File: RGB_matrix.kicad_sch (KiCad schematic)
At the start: 117 parts

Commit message: some layouts done
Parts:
- removed D100, D101, D102, D103, D104, D105, D106, D107, D108, D109, D110, D111, D112, D113, D114, D115, D116, D117, D118, D119, D120, D121, D122, D123, D124, D125, D126, D127, D128, D129, D130, D131, D132, D133, D134, D135, D136, D137, D138, D139, D140, D141, D142, D143, D144, D145, D146, D147, D148, D149, D150, D151, D152, D153, D154, D155, D156, D157, D158, D159, D160, D161, D162, D163, D164, D165, D166, D167, D168, D169, D170, D171, D172, D173, D174, D175, D176, D177, D178, D179, D180, D181, D182, D183, D184, D185, D186, D187, D188, D189, D190, D191, D192, D193, D194, D195, D196, D197, D198, D199, D200, D201, D202, D203, D204, D205, D98, D99: LED_ABGR, symbol Device:LED_ABGR
- added RGB10, RGB11, RGB12, RGB13, RGB14, RGB15, RGB16, RGB17, RGB18, RGB19, RGB20, RGB21, RGB22, RGB23, RGB24, RGB25, RGB26, RGB27, RGB28, RGB29, RGB30, RGB31, RGB32, RGB33, RGB34, RGB35, RGB36, RGB37, RGB38, RGB39, RGB40, RGB41, RGB42, RGB43, RGB44, RGB45, RGB46, RGB47, RGB48, RGB49, RGB50, RGB51, RGB52, RGB53, RGB54, RGB55, RGB56, RGB57, RGB58, RGB59, RGB60, RGB61, RGB62, RGB63, RGB64, RGB65, RGB66, RGB67, RGB68, RGB69, RGB70, RGB71, RGB72, RGB73, RGB74, RGB75, RGB76, RGB77, RGB78, RGB79, RGB80, RGB82, RGB83, RGB84, RGB85, RGB86, RGB87, RGB88: LED_ABGR, marbastlib-various:MHT151RGBCT-RGB-Reverse-Mount-1206, symbol Device:LED_ABGR
- RGB1: renamed from D89; footprint (none) -> marbastlib-various:MHT151RGBCT-RGB-Reverse-Mount-1206
- RGB2: renamed from D90; footprint (none) -> marbastlib-various:MHT151RGBCT-RGB-Reverse-Mount-1206
- RGB3: renamed from D91; footprint (none) -> marbastlib-various:MHT151RGBCT-RGB-Reverse-Mount-1206
- RGB4: renamed from D92; footprint (none) -> marbastlib-various:MHT151RGBCT-RGB-Reverse-Mount-1206
- RGB5: renamed from D93; footprint (none) -> marbastlib-various:MHT151RGBCT-RGB-Reverse-Mount-1206
- RGB6: renamed from D94; footprint (none) -> marbastlib-various:MHT151RGBCT-RGB-Reverse-Mount-1206
- RGB7: renamed from D95; footprint (none) -> marbastlib-various:MHT151RGBCT-RGB-Reverse-Mount-1206
- RGB8: renamed from D96; footprint (none) -> marbastlib-various:MHT151RGBCT-RGB-Reverse-Mount-1206
- RGB9: renamed from D97; footprint (none) -> marbastlib-various:MHT151RGBCT-RGB-Reverse-Mount-1206
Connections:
- net CS4: now also RGB10.4 (RK), RGB11.4 (RK), RGB12.4 (RK), RGB13.4 (RK), RGB14.4 (RK), RGB15.4 (RK), RGB16.4 (RK), RGB17.4 (RK), RGB18.4 (RK)
- net CS5: now also RGB10.3 (GK), RGB11.3 (GK), RGB12.3 (GK), RGB13.3 (GK), RGB14.3 (GK), RGB15.3 (GK), RGB16.3 (GK), RGB17.3 (GK), RGB18.3 (GK)
- net CS6: now also RGB10.2 (BK), RGB11.2 (BK), RGB12.2 (BK), RGB13.2 (BK), RGB14.2 (BK), RGB15.2 (BK), RGB16.2 (BK), RGB17.2 (BK), RGB18.2 (BK)
- net SW1: now also RGB10.1 (A), RGB19.1 (A), RGB28.1 (A), RGB37.1 (A), RGB46.1 (A), RGB55.1 (A), RGB64.1 (A), RGB73.1 (A), RGB83.1 (A)
- net SW2: now also RGB11.1 (A), RGB20.1 (A), RGB29.1 (A), RGB38.1 (A), RGB47.1 (A), RGB56.1 (A), RGB65.1 (A), RGB74.1 (A), RGB84.1 (A)
- net SW3: now also RGB12.1 (A), RGB21.1 (A), RGB30.1 (A), RGB39.1 (A), RGB48.1 (A), RGB57.1 (A), RGB66.1 (A), RGB75.1 (A), RGB85.1 (A)
- net SW4: now also RGB13.1 (A), RGB22.1 (A), RGB31.1 (A), RGB40.1 (A), RGB49.1 (A), RGB58.1 (A), RGB67.1 (A), RGB76.1 (A), RGB86.1 (A)
- net SW5: now also RGB14.1 (A), RGB23.1 (A), RGB32.1 (A), RGB41.1 (A), RGB50.1 (A), RGB59.1 (A), RGB68.1 (A), RGB77.1 (A), RGB87.1 (A)
- net SW6: now also RGB15.1 (A), RGB24.1 (A), RGB33.1 (A), RGB42.1 (A), RGB51.1 (A), RGB60.1 (A), RGB69.1 (A), RGB78.1 (A), RGB88.1 (A)
- net SW7: now also RGB16.1 (A), RGB25.1 (A), RGB34.1 (A), RGB43.1 (A), RGB52.1 (A), RGB61.1 (A), RGB70.1 (A), RGB79.1 (A)
- net SW8: now also RGB17.1 (A), RGB26.1 (A), RGB35.1 (A), RGB44.1 (A), RGB53.1 (A), RGB62.1 (A), RGB71.1 (A), RGB80.1 (A)
- net SW9: now also RGB18.1 (A), RGB27.1 (A), RGB36.1 (A), RGB45.1 (A), RGB54.1 (A), RGB63.1 (A), RGB72.1 (A), RGB82.1 (A)
- new net CS10: RGB28.4 (RK), RGB29.4 (RK), RGB30.4 (RK), RGB31.4 (RK), RGB32.4 (RK), RGB33.4 (RK), RGB34.4 (RK), RGB35.4 (RK), RGB36.4 (RK)
- new net CS11: RGB28.3 (GK), RGB29.3 (GK), RGB30.3 (GK), RGB31.3 (GK), RGB32.3 (GK), RGB33.3 (GK), RGB34.3 (GK), RGB35.3 (GK), RGB36.3 (GK)
- new net CS12: RGB28.2 (BK), RGB29.2 (BK), RGB30.2 (BK), RGB31.2 (BK), RGB32.2 (BK), RGB33.2 (BK), RGB34.2 (BK), RGB35.2 (BK), RGB36.2 (BK)
- new net CS13: RGB37.4 (RK), RGB38.4 (RK), RGB39.4 (RK), RGB40.4 (RK), RGB41.4 (RK), RGB42.4 (RK), RGB43.4 (RK), RGB44.4 (RK), RGB45.4 (RK)
- new net CS14: RGB37.3 (GK), RGB38.3 (GK), RGB39.3 (GK), RGB40.3 (GK), RGB41.3 (GK), RGB42.3 (GK), RGB43.3 (GK), RGB44.3 (GK), RGB45.3 (GK)
- new net CS15: RGB37.2 (BK), RGB38.2 (BK), RGB39.2 (BK), RGB40.2 (BK), RGB41.2 (BK), RGB42.2 (BK), RGB43.2 (BK), RGB44.2 (BK), RGB45.2 (BK)
- new net CS16: RGB46.4 (RK), RGB47.4 (RK), RGB48.4 (RK), RGB49.4 (RK), RGB50.4 (RK), RGB51.4 (RK), RGB52.4 (RK), RGB53.4 (RK), RGB54.4 (RK)
- new net CS17: RGB46.3 (GK), RGB47.3 (GK), RGB48.3 (GK), RGB49.3 (GK), RGB50.3 (GK), RGB51.3 (GK), RGB52.3 (GK), RGB53.3 (GK), RGB54.3 (GK)
- new net CS18: RGB46.2 (BK), RGB47.2 (BK), RGB48.2 (BK), RGB49.2 (BK), RGB50.2 (BK), RGB51.2 (BK), RGB52.2 (BK), RGB53.2 (BK), RGB54.2 (BK)
- new net CS19: RGB55.4 (RK), RGB56.4 (RK), RGB57.4 (RK), RGB58.4 (RK), RGB59.4 (RK), RGB60.4 (RK), RGB61.4 (RK), RGB62.4 (RK), RGB63.4 (RK)
- new net CS20: RGB55.3 (GK), RGB56.3 (GK), RGB57.3 (GK), RGB58.3 (GK), RGB59.3 (GK), RGB60.3 (GK), RGB61.3 (GK), RGB62.3 (GK), RGB63.3 (GK)
- new net CS21: RGB55.2 (BK), RGB56.2 (BK), RGB57.2 (BK), RGB58.2 (BK), RGB59.2 (BK), RGB60.2 (BK), RGB61.2 (BK), RGB62.2 (BK), RGB63.2 (BK)
- new net CS22: RGB64.4 (RK), RGB65.4 (RK), RGB66.4 (RK), RGB67.4 (RK), RGB68.4 (RK), RGB69.4 (RK), RGB70.4 (RK), RGB71.4 (RK), RGB72.4 (RK)
- new net CS23: RGB64.3 (GK), RGB65.3 (GK), RGB66.3 (GK), RGB67.3 (GK), RGB68.3 (GK), RGB69.3 (GK), RGB70.3 (GK), RGB71.3 (GK), RGB72.3 (GK)
- new net CS24: RGB64.2 (BK), RGB65.2 (BK), RGB66.2 (BK), RGB67.2 (BK), RGB68.2 (BK), RGB69.2 (BK), RGB70.2 (BK), RGB71.2 (BK), RGB72.2 (BK)
- new net CS25: RGB73.4 (RK), RGB74.4 (RK), RGB75.4 (RK), RGB76.4 (RK), RGB77.4 (RK), RGB78.4 (RK), RGB79.4 (RK), RGB80.4 (RK), RGB82.4 (RK)
- new net CS26: RGB73.3 (GK), RGB74.3 (GK), RGB75.3 (GK), RGB76.3 (GK), RGB77.3 (GK), RGB78.3 (GK), RGB79.3 (GK), RGB80.3 (GK), RGB82.3 (GK)
- new net CS27: RGB73.2 (BK), RGB74.2 (BK), RGB75.2 (BK), RGB76.2 (BK), RGB77.2 (BK), RGB78.2 (BK), RGB79.2 (BK), RGB80.2 (BK), RGB82.2 (BK)
- new net CS28: RGB83.4 (RK), RGB84.4 (RK), RGB85.4 (RK), RGB86.4 (RK), RGB87.4 (RK), RGB88.4 (RK)
- new net CS29: RGB83.3 (GK), RGB84.3 (GK), RGB85.3 (GK), RGB86.3 (GK), RGB87.3 (GK), RGB88.3 (GK)
- new net CS30: RGB83.2 (BK), RGB84.2 (BK), RGB85.2 (BK), RGB86.2 (BK), RGB87.2 (BK), RGB88.2 (BK)
- new net CS7: RGB19.4 (RK), RGB20.4 (RK), RGB21.4 (RK), RGB22.4 (RK), RGB23.4 (RK), RGB24.4 (RK), RGB25.4 (RK), RGB26.4 (RK), RGB27.4 (RK)
- new net CS8: RGB19.3 (GK), RGB20.3 (GK), RGB21.3 (GK), RGB22.3 (GK), RGB23.3 (GK), RGB24.3 (GK), RGB25.3 (GK), RGB26.3 (GK), RGB27.3 (GK)
- new net CS9: RGB19.2 (BK), RGB20.2 (BK), RGB21.2 (BK), RGB22.2 (BK), RGB23.2 (BK), RGB24.2 (BK), RGB25.2 (BK), RGB26.2 (BK), RGB27.2 (BK)

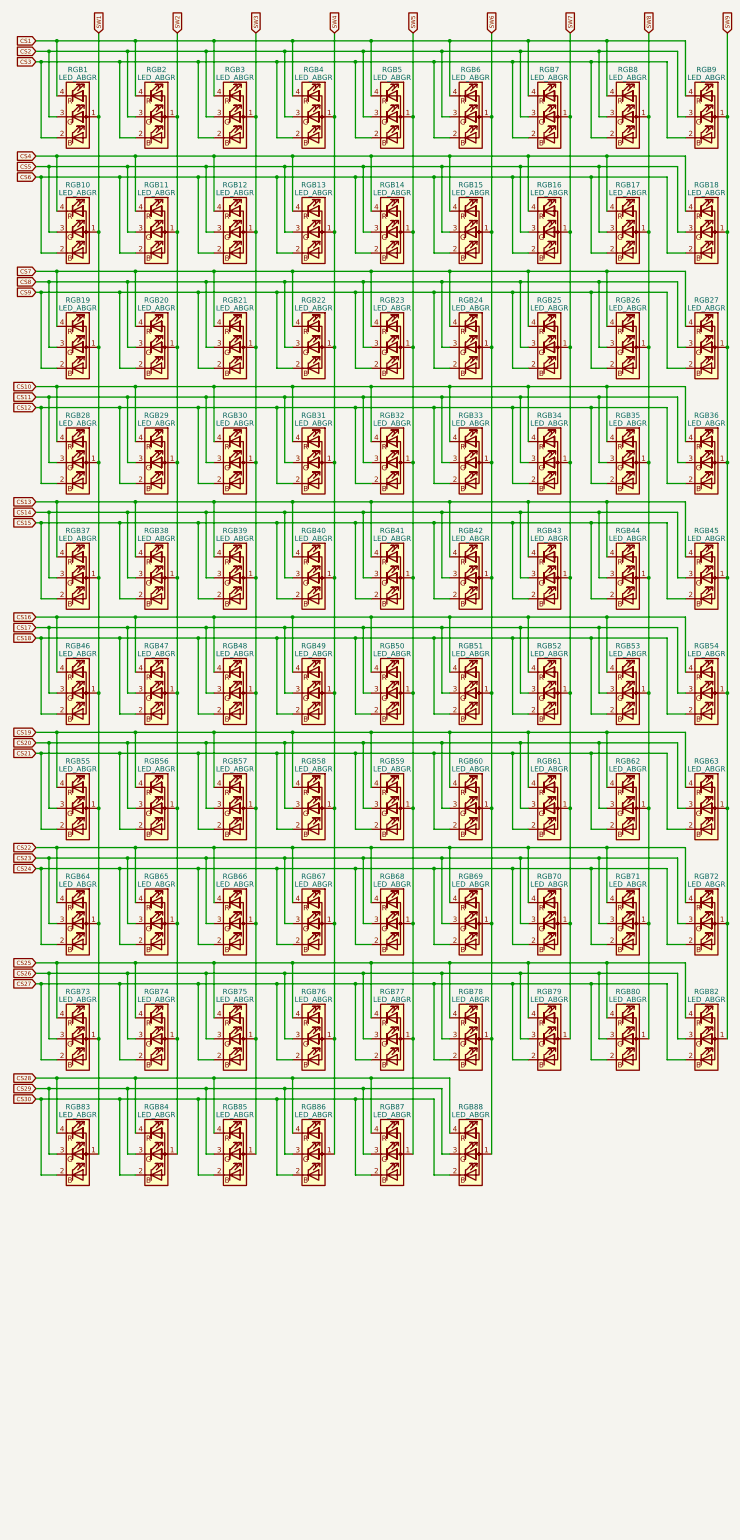
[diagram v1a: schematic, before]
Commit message: improved rgb schematic
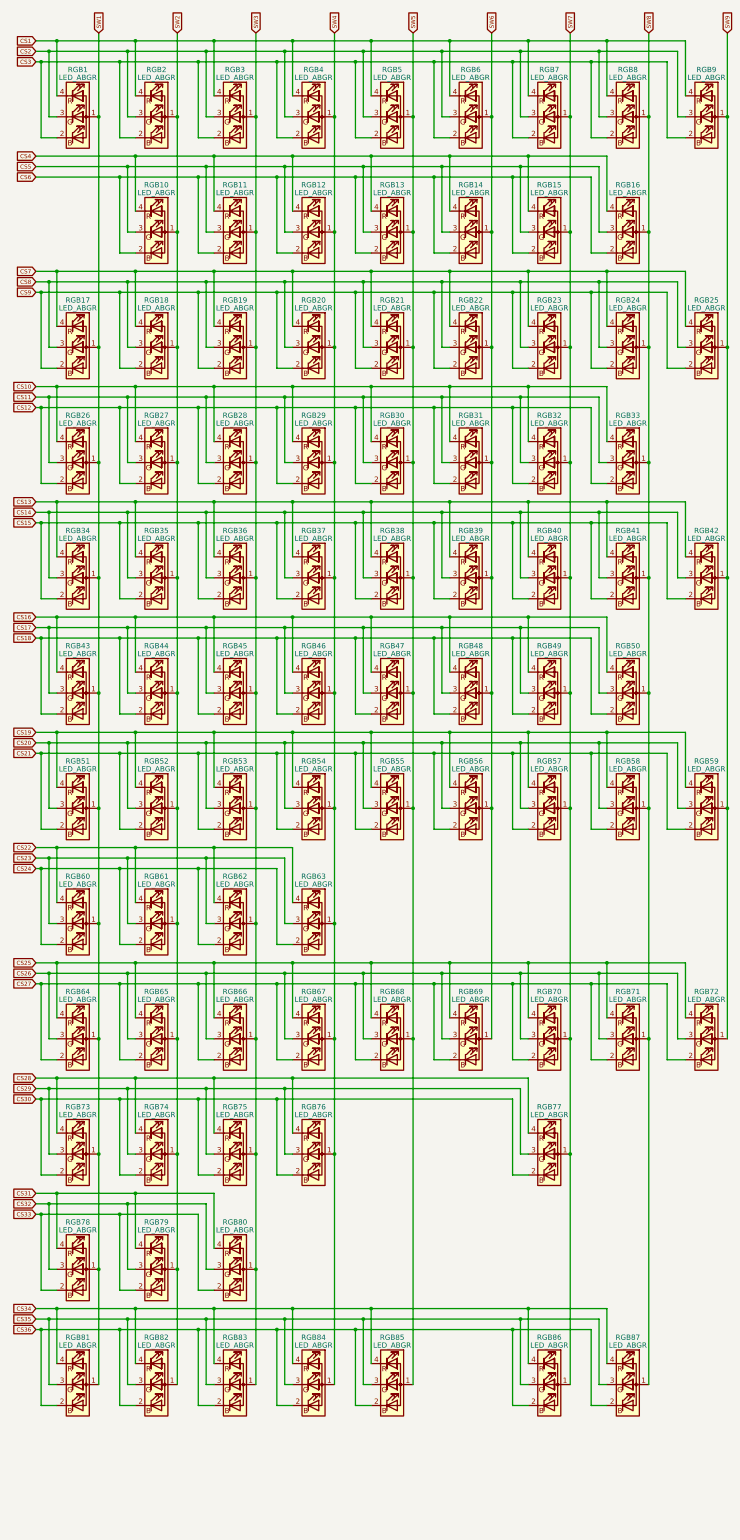
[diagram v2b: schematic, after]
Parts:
- removed RGB10, RGB18, RGB36, RGB54, RGB73, RGB74, RGB75, RGB76, RGB88: LED_ABGR, marbastlib-various:MHT151RGBCT-RGB-Reverse-Mount-1206, symbol Device:LED_ABGR
- added RGB63, RGB64, RGB65, RGB66, RGB81, RGB83, RGB84, RGB85, RGB86: LED_ABGR, marbastlib-various:MHT151RGBCT-RGB-Reverse-Mount-1206, symbol Device:LED_ABGR
- renumbered RGB11 to RGB10, RGB12 to RGB11, RGB13 to RGB12, RGB14 to RGB13, RGB15 to RGB14, RGB16 to RGB15, RGB17 to RGB16, RGB19 to RGB17, RGB20 to RGB18, RGB21 to RGB19, RGB22 to RGB20, RGB23 to RGB21, RGB24 to RGB22, RGB25 to RGB23, RGB26 to RGB24, RGB27 to RGB25, RGB28 to RGB26, RGB29 to RGB27, RGB30 to RGB28, RGB31 to RGB29, RGB32 to RGB30, RGB33 to RGB31, RGB34 to RGB32, RGB35 to RGB33, RGB37 to RGB34, RGB38 to RGB35, RGB39 to RGB36, RGB40 to RGB37, RGB41 to RGB38, RGB42 to RGB39, RGB43 to RGB40, RGB44 to RGB41, RGB45 to RGB42, RGB46 to RGB43, RGB47 to RGB44, RGB48 to RGB45, RGB49 to RGB46, RGB50 to RGB47, RGB51 to RGB48, RGB52 to RGB49, RGB53 to RGB50, RGB55 to RGB51, RGB56 to RGB52, RGB57 to RGB53, RGB58 to RGB54, RGB59 to RGB55, RGB60 to RGB56, RGB61 to RGB57, RGB62 to RGB58, RGB63 to RGB59, RGB64 to RGB60, RGB65 to RGB61, RGB66 to RGB62, RGB83 to RGB73, RGB84 to RGB74, RGB85 to RGB75, RGB86 to RGB76
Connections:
- net CS22: now also RGB63.4 (RK); no longer RGB67.4 (RK), RGB68.4 (RK), RGB69.4 (RK), RGB70.4 (RK), RGB71.4 (RK), RGB72.4 (RK)
- net CS23: now also RGB63.3 (GK); no longer RGB67.3 (GK), RGB68.3 (GK), RGB69.3 (GK), RGB70.3 (GK), RGB71.3 (GK), RGB72.3 (GK)
- net CS24: now also RGB63.2 (BK); no longer RGB67.2 (BK), RGB68.2 (BK), RGB69.2 (BK), RGB70.2 (BK), RGB71.2 (BK), RGB72.2 (BK)
- net CS25: now also RGB67.4 (RK), RGB68.4 (RK), RGB69.4 (RK), RGB70.4 (RK), RGB71.4 (RK), RGB72.4 (RK), RGB64.4 (RK), RGB65.4 (RK), RGB66.4 (RK); no longer RGB77.4 (RK), RGB78.4 (RK), RGB79.4 (RK), RGB80.4 (RK), RGB82.4 (RK)
- net CS26: now also RGB67.3 (GK), RGB68.3 (GK), RGB69.3 (GK), RGB70.3 (GK), RGB71.3 (GK), RGB72.3 (GK), RGB64.3 (GK), RGB65.3 (GK), RGB66.3 (GK); no longer RGB77.3 (GK), RGB78.3 (GK), RGB79.3 (GK), RGB80.3 (GK), RGB82.3 (GK)
- net CS27: now also RGB67.2 (BK), RGB68.2 (BK), RGB69.2 (BK), RGB70.2 (BK), RGB71.2 (BK), RGB72.2 (BK), RGB64.2 (BK), RGB65.2 (BK), RGB66.2 (BK); no longer RGB77.2 (BK), RGB78.2 (BK), RGB79.2 (BK), RGB80.2 (BK), RGB82.2 (BK)
- net CS28: now also RGB77.4 (RK); no longer RGB87.4 (RK)
- net CS29: now also RGB77.3 (GK); no longer RGB87.3 (GK)
- net CS30: now also RGB77.2 (BK); no longer RGB87.2 (BK)
- net SW1: now also RGB78.1 (A), RGB64.1 (A), RGB81.1 (A)
- net SW2: now also RGB79.1 (A), RGB82.1 (A), RGB65.1 (A)
- net SW3: now also RGB80.1 (A), RGB66.1 (A), RGB83.1 (A)
- net SW4: now also RGB63.1 (A), RGB84.1 (A)
- net SW5: now also RGB85.1 (A); no longer RGB77.1 (A), RGB87.1 (A)
- net SW6: no longer RGB78.1 (A)
- net SW7: now also RGB77.1 (A), RGB86.1 (A); no longer RGB79.1 (A)
- net SW8: now also RGB87.1 (A); no longer RGB80.1 (A)
- net SW9: no longer RGB82.1 (A)
- new net CS31: RGB78.4 (RK), RGB79.4 (RK), RGB80.4 (RK)
- new net CS32: RGB78.3 (GK), RGB79.3 (GK), RGB80.3 (GK)
- new net CS33: RGB78.2 (BK), RGB79.2 (BK), RGB80.2 (BK)
- new net CS34: RGB81.4 (RK), RGB82.4 (RK), RGB83.4 (RK), RGB84.4 (RK), RGB85.4 (RK), RGB86.4 (RK), RGB87.4 (RK)
- new net CS35: RGB81.3 (GK), RGB82.3 (GK), RGB83.3 (GK), RGB84.3 (GK), RGB85.3 (GK), RGB86.3 (GK), RGB87.3 (GK)
- new net CS36: RGB81.2 (BK), RGB82.2 (BK), RGB83.2 (BK), RGB84.2 (BK), RGB85.2 (BK), RGB86.2 (BK), RGB87.2 (BK)

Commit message: small fixes
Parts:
- renumbered RGB3 to RGB2, RGB4 to RGB3, RGB5 to RGB4, RGB6 to RGB5, RGB7 to RGB6, RGB8 to RGB7, RGB9 to RGB8, RGB2 to RGB9
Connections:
- net CS1: no longer RGB9.4 (RK)
- net CS2: no longer RGB9.3 (GK)
- net CS3: no longer RGB9.2 (BK)
- net CS4: now also RGB9.4 (RK)
- net CS5: now also RGB9.3 (GK)
- net CS6: now also RGB9.2 (BK)
- net SW1: now also RGB9.1 (A)
- net SW2: no longer RGB9.1 (A)
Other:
- moved on the sheet: RGB9
